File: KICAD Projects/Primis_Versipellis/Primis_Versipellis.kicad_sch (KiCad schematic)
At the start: 28 parts, among them J1 USB-05, J3 Conn_01x05_Pin, U1 nRF52833_QDxx, Y2 Crystal_GND24

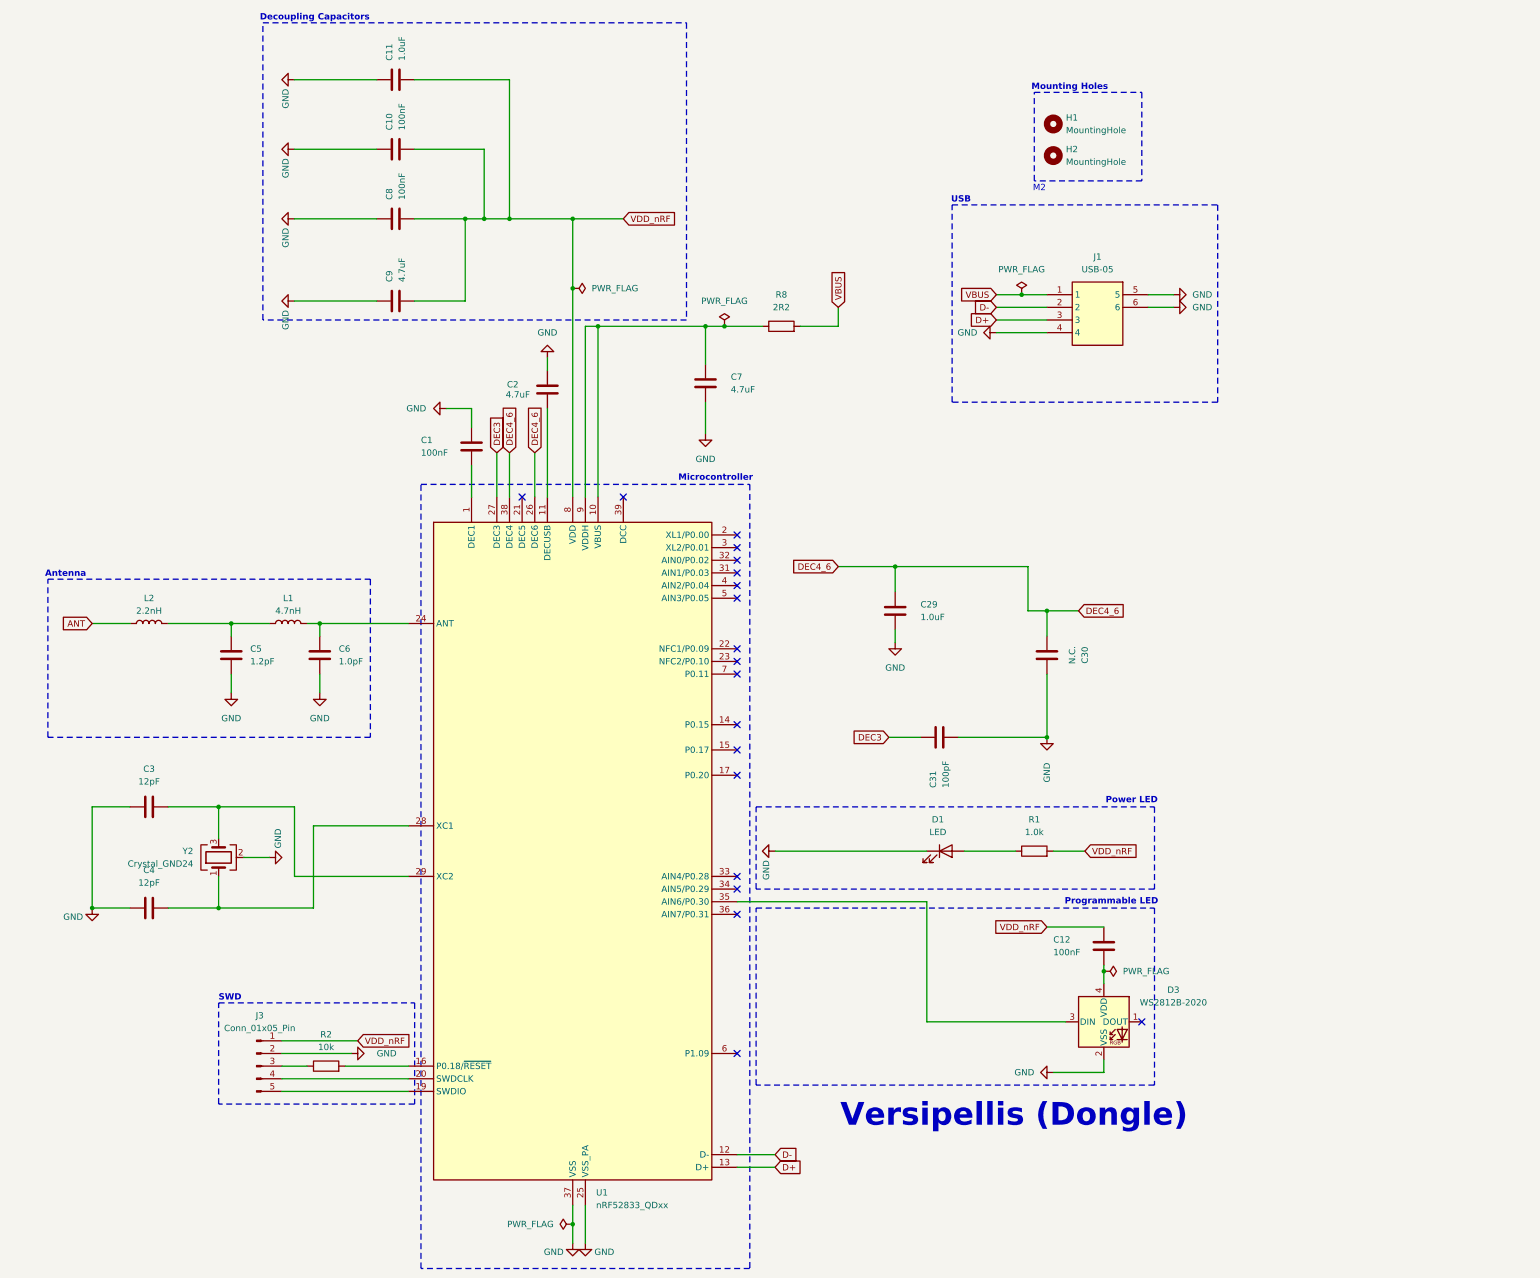
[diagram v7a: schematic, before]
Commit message: VERSIPELLIS EV2 + TURRIM Production files
-Swapped to a tag connect for programming VERSIPELLIS
-Moved crystal closer to the NRF on VERSIPELLIS
-Fixed swapped lines on usb on VERSIPELLIS
-TURRIM cleanup and production files added
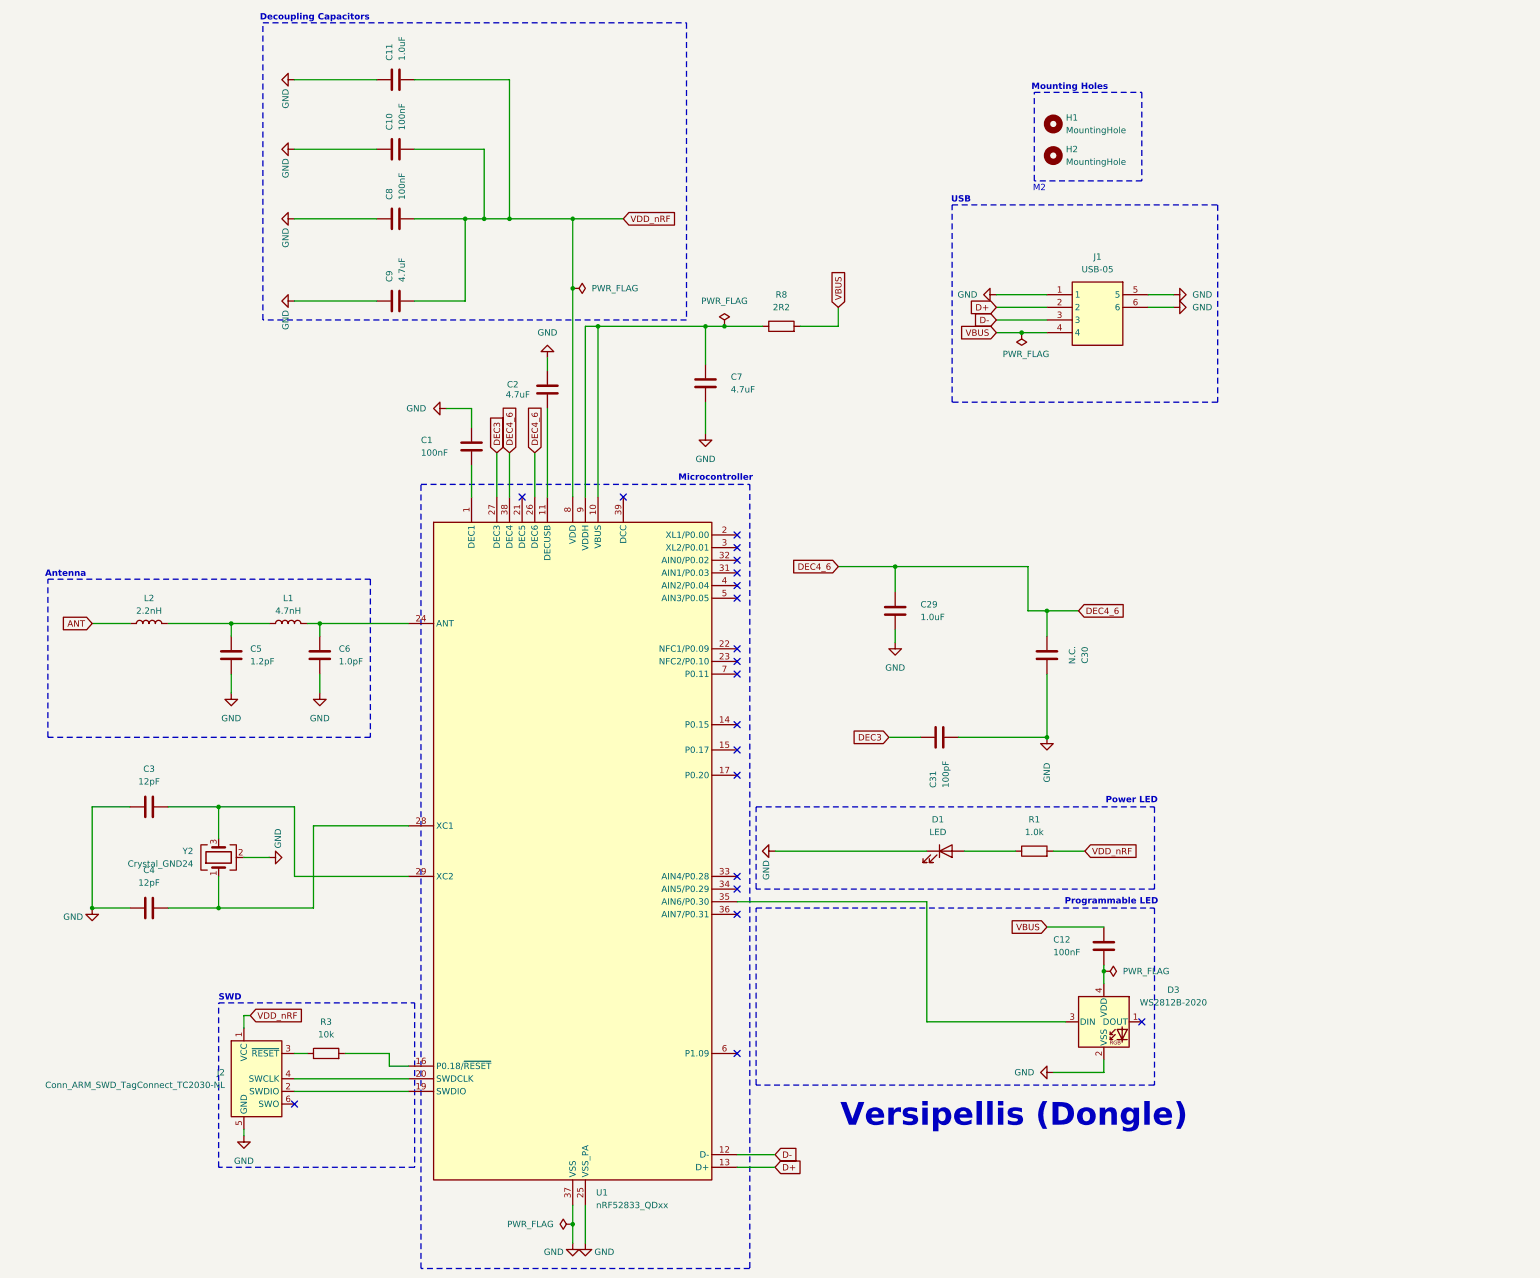
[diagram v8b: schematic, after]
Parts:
- removed J3: Conn_01x05_Pin, Connector_PinHeader_1.27mm:PinHeader_1x05_P1.27mm_Vertical, symbol Connector:Conn_01x05_Pin
- removed R2: 10k, Resistor_SMD:R_0603_1608Metric, symbol Device:R
- added J2: Conn_ARM_SWD_TagConnect_TC2030-NL, Connector:Tag-Connect_TC2030-IDC-NL_2x03_P1.27mm_Vertical, symbol Connector:Conn_ARM_SWD_TagConnect_TC2030-NL
- added R3: 10k, Resistor_SMD:R_0603_1608Metric, symbol Device:R
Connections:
- net D+: now also J1.2; no longer J1.3
- net D-: now also J1.3; no longer J1.2
- net GND: now also J1.1, J2.5 (GND); no longer J1.4
- net VBUS: now also C12.1, J1.4; no longer J1.1
- net VDD_nRF: now also J2.1 (VCC); no longer C12.1
- net at U1.16 (P0.18/~{RESET}): now also R3.2
- net at U1.19 (SWDIO): now also J2.2 (SWDIO)
- net at U1.20 (SWDCLK): now also J2.4 (SWCLK)
- new net: J2.3 (~{RESET}), R3.1
- no-connect marks 19 -> 20
